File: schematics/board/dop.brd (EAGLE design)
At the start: 65.8 x 65.8 mm, 75 parts, among them X1 53047-02

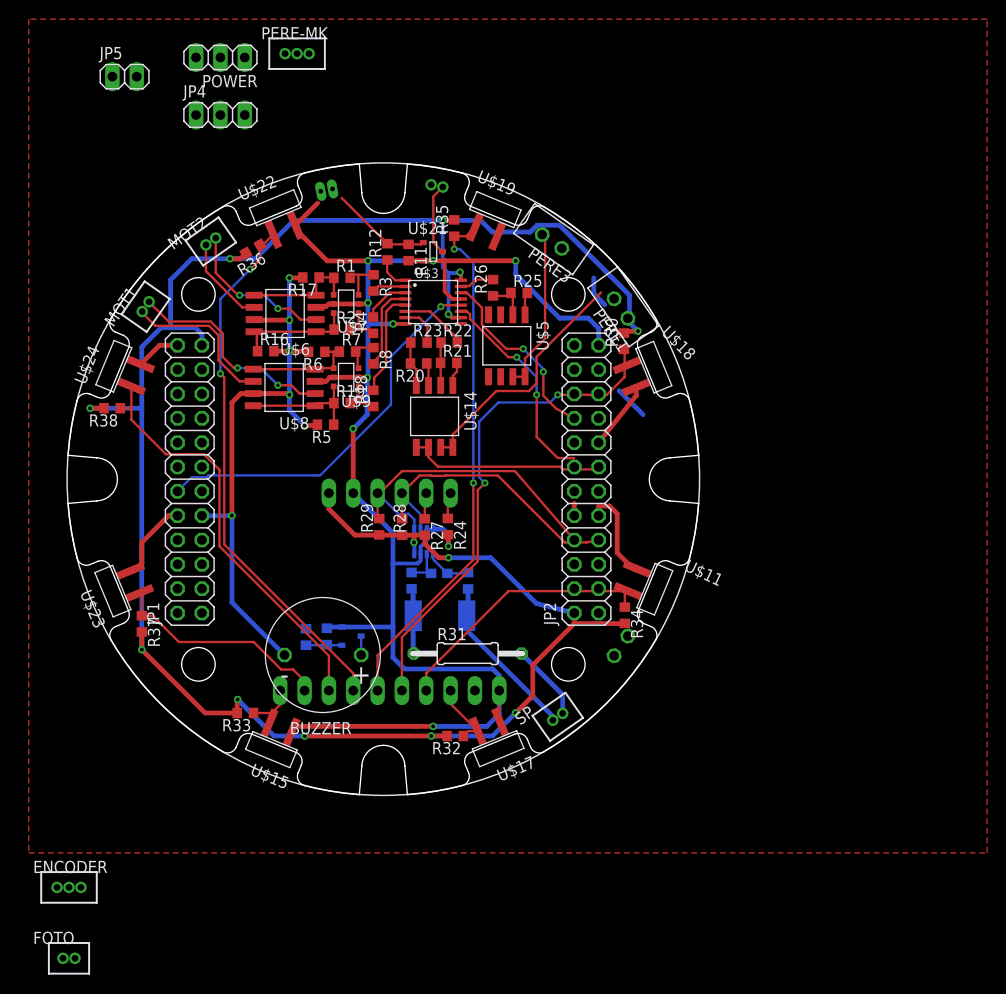
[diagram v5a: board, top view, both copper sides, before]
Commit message: Доделаны платы dop и mtr
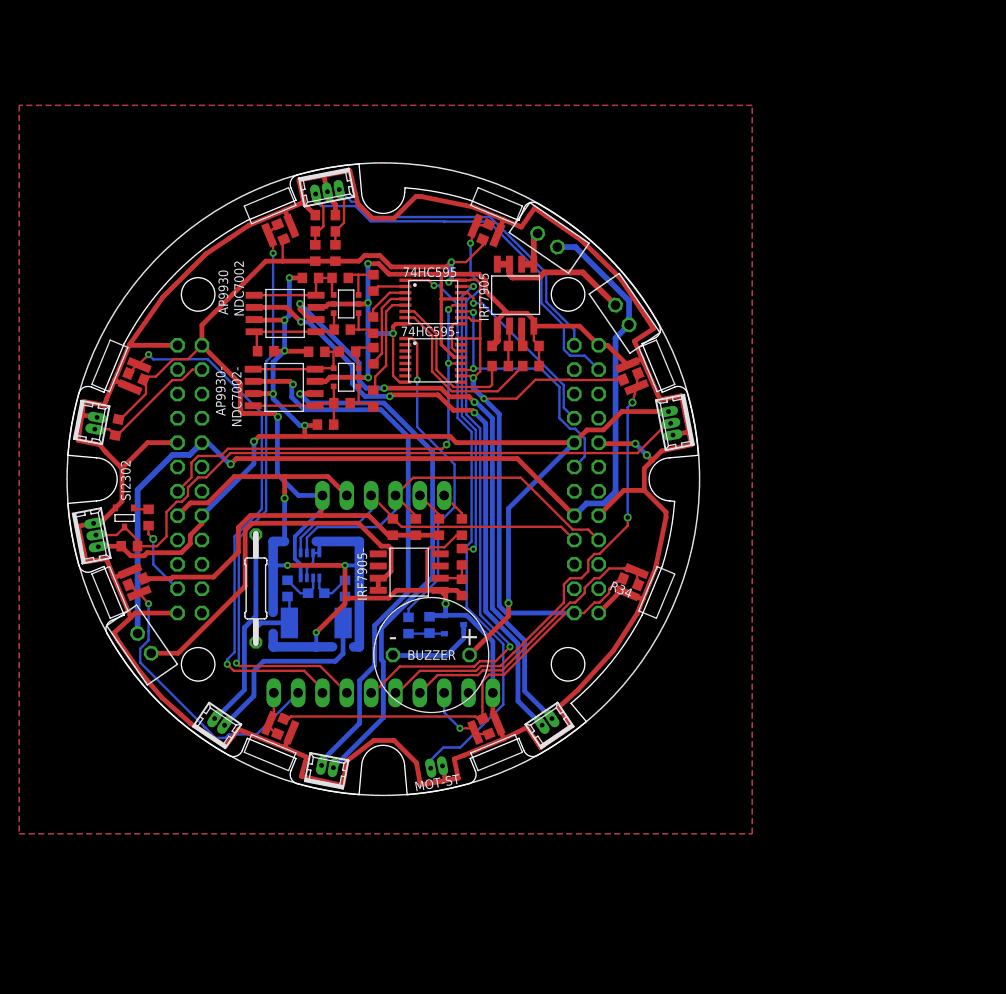
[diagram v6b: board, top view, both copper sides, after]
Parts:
- removed FOTO, MOT1, MOT2, MOT3: JST_2CON, CanCubeSat:JST_2CON_1.25
- removed JP4, POWER: (no value), pinhead:1X03
- removed JP5: (no value), pinhead:1X02
- removed PERE-MK: JST_3CON, CanCubeSat:JST_3CON_1.25
- removed PERE1, PERE2, PERE3: JST-2-2.5, CanCubeSat:JST-2-2.5
- removed U$14, U$5: IRF7905, CanCubeSat:SO8
- removed U$16: AD5593, CanCubeSat:AD5593
- removed U$2: INA219AID, CanCubeSat:INA219AID
- removed U$20, U$21: SI2302CDS, CanCubeSat:SI2302CDS
- removed U$3: 74HC595, CanCubeSat:74HC595
- removed X1: 53047-02, con-molex:53047-02
- added 74HC595, 74HC595-: 74HC595, CanCubeSat:TSSOP16
- added AD5593: AD5593, CanCubeSat:AD5593
- added C2, C3: 100nF, rcl:C0603
- added INA: INA219AID, CanCubeSat:SOT23-8
- added IRF7905, IRF7905-: IRF7905, CanCubeSat:SO8
- added LED, LED1: MOLEX-3-1.25, CanCubeSat:53047-03
- added MOT-H, MOT-ST, MOT-V, PHOTO: MOLEX-2-1.25, CanCubeSat:53047-02
- added PER-PAR, PER-SP, PER-ST: JST-2-2.5, CanCubeSat:JST-2-2.5
- added R39: 2k, rcl:R0603
- added R41: 100R, rcl:R0603
- added R42: 4k7, rcl:R0603
- added SI2302, SI2302-: SI2302CDS, CanCubeSat:SOT23-3
- ENCODER: value JST_3CON -> MOLEX-3-1.25; device CanCubeSat:JST_3CON_1.25 -> CanCubeSat:53047-03
- R11: value 10k -> 5k1
- R12: value 1k -> 5k1
- R16: value 10k -> 10k*3
- SP: value JST_2CON -> MOLEX-2-1.25; device CanCubeSat:JST_2CON_1.25 -> CanCubeSat:53047-02
- U$11, U$15, U$17, U$18, U$19, U$22, U$23, U$24: device CanCubeSat:VT93N1 -> KNPN-2023:VT93N1
- moved ENCODER 77.8 mm to (27.1, 63.4), turned to 191 degrees
- moved SP 35.5 mm to (15.7, 7.30), turned to 326 degrees
- moved R25 31.3 mm to (41.2, 21.7), turned to 270 degrees
- moved R26 28.3 mm to (41.2, 24.9)
- moved R31 23.1 mm to (19.7, 21.6), turned to 90 degrees
- moved C1 13.0 mm to (26.0, 21.1)
- moved R14 13.0 mm to (23.0, 21.6)
- moved R15 12.9 mm to (26.0, 18.0)
- moved R13 12.9 mm to (29.0, 21.6)
- moved R23 11.9 mm to (48.4, 44.8), turned to 180 degrees
- moved R20 11.9 mm to (48.4, 46.9), turned to 0 degrees
- moved BUZZER 11.3 mm to (38.0, 14.7), turned to 0 degrees
- moved R10 10.8 mm to (35.6, 17.7)
- moved R9 10.8 mm to (37.8, 17.8)
- moved R11 9.73 mm to (25.9, 56.6)
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- renumbered JP1 to A, JP2 to B, U$6 to AP9930, U$7 to NDC7002, U$8 to AP9930-, U$9 to NDC7002-
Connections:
- removed net ADC: JP5.2
- removed net CSK: JP4.2
- removed net ENCOD_C: ENCODER.1
- removed net FOTO_G: FOTO.3
- removed net FOTO_R: FOTO.2
- removed net I2C: JP5.1
- removed net MOTOR3-: MOT3.3, U$21.3
- removed net N$10: R21.2, U$14.1
- removed net N$11: R20.2, R23.1, U$14.4
- removed net N$19: R25.2, U$5.1
- removed net PA4: B.21
- removed net PA5: B.24
- removed net PA7: A.21
- removed net PA8: A.4
- new net FOTO9: A.22, PHOTO.1, R39.1
- new net LED: A.3, R41.1
- new net N$22: 74HC595-.14, 74HC595.9
- new net N$23: LED.2, LED1.2, R42.2, SI2302.3
- net 3V3: now also 74HC595-.10, 74HC595-.16, 74HC595.10, 74HC595.16, A.24, AD5593.16, B.1, INA.4, R11.2, R12.2, R39.2; no longer A.23, B.2, POWER.2, U$16.16, U$2.4, U$3.10, U$3.16
- net 5V: now also A.10, B.15, LED.1, LED1.1, R42.1; no longer A.9, B.16, POWER.1
- net BUZZER: now also 74HC595-.1
- net ENCOD_A: now also B.22, C3.2, ENCODER.1, R11.1; no longer ENCODER.2
- net ENCOD_B: now also B.23, C2.2, R12.1
- net FOTO1: now also AD5593.3; no longer U$16.3
- net FOTO2: now also AD5593.4, U$11.P$1; no longer U$11.P$2, U$16.4
- net FOTO3: now also AD5593.5, U$18.P$2; no longer U$16.5, U$18.P$1
- net FOTO4: now also AD5593.6; no longer U$16.6
- net FOTO5: now also AD5593.7; no longer U$16.7
- net FOTO6: now also AD5593.8, U$24.P$2; no longer U$16.8, U$24.P$1
- net FOTO7: now also AD5593.9; no longer U$16.9
- net FOTO8: now also AD5593.10; no longer U$16.10
- net GND: now also 74HC595-.13, 74HC595-.8, 74HC595.13, 74HC595.8, A.1, A.15, A.23, A.9, AD5593.1, AD5593.15, B.10, B.16, B.2, B.24, C2.1, C3.1, ENCODER.2, INA.3, INA.7, INA.8, IRF7905-.1, IRF7905.1, IRF7905.4, LED.3, LED1.3, MOT-ST.2, PHOTO.2, R20.2, R21.2, R23.1, R25.2, SI2302-.2, SI2302.2, U$11.P$2, U$18.P$1, U$24.P$1; no longer A.10, A.16, A.2, A.24, B.1, B.15, B.23, B.9, POWER.3, R11.2, U$11.P$1, U$16.1, U$16.15, U$18.P$2, U$2.3, U$2.7, U$2.8, U$20.2, U$21.2, U$24.P$2, U$3.13, U$3.8, X1.1
- net LATCH: now also 74HC595-.12, 74HC595.12, A.11; no longer A.12, JP4.3, U$3.12
- net MISO: now also B.18; no longer B.17
- net MK_MOTOR1+: now also 74HC595.4; no longer U$3.4
- net MK_MOTOR1-: now also 74HC595.5; no longer U$3.5
- net MK_MOTOR2+: now also 74HC595.2; no longer U$3.2
- net MK_MOTOR2-: now also 74HC595.3; no longer U$3.3
- net MOSI: now also 74HC595.14, B.17; no longer B.18, JP4.1, U$3.14
- net MOTOR1+: now also MOT-H.2; no longer MOT1.2
- net MOTOR1-: now also MOT-H.1; no longer MOT1.3
- net MOTOR2+: now also MOT-V.2; no longer MOT2.2
- net MOTOR2-: now also MOT-V.1; no longer MOT2.3
- net N$12: now also IRF7905.2; no longer U$14.2
- net N$13: now also SI2302-.3; no longer U$20.3
- net N$14: now also SI2302-.1; no longer U$20.1
- net N$15: now also INA.1; no longer U$2.1
- net N$16: now also INA.2; no longer U$2.2
- net N$17: now also R41.2, SI2302.1; no longer R11.1, R12.2, U$21.1, X1.2
- net N$18: now also AD5593.12; no longer U$16.12
- net N$20: now also AD5593.11; no longer U$16.11
- net N$21: now also IRF7905-.2; no longer U$5.2
- net N$9: now also IRF7905.3; no longer U$14.3
- net PA6: now also A.21; no longer A.22
- net PC5: now also A.20; no longer A.19
- net PERE1: now also 74HC595.6; no longer PERE-MK.2, U$3.6
- net PERE1_G: now also IRF7905.7, IRF7905.8, PER-PAR.1; no longer PERE1.1, U$14.7, U$14.8
- net PERE2: now also 74HC595.7; no longer PERE-MK.3, U$3.7
- net PERE2_G: now also IRF7905.5, IRF7905.6, PER-ST.1; no longer PERE2.2, U$14.5, U$14.6
- net PERE3: now also 74HC595.15; no longer PERE-MK.1, U$3.15
- net PERE3_G: now also IRF7905-.7, IRF7905-.8, PER-SP.1; no longer PERE3.1, U$5.7, U$5.8
- net SCK: now also 74HC595-.11, 74HC595.11, B.13; no longer B.14, U$3.11
- net SCL: now also AD5593.14, B.7, INA.5; no longer B.8, U$16.14, U$2.5
- net SDA: now also AD5593.13, B.8, INA.6; no longer B.7, U$16.13, U$2.6
- net SP+: now also SP.1; no longer SP.2
- net SP-: now also SP.2; no longer SP.3
- net TRUBKI: now also 74HC595.1, MOT-ST.1; no longer R12.1, U$3.1
- net VAB: now also A.16, B.9, PER-PAR.2, PER-SP.2, PER-ST.2; no longer A.15, B.10, PERE1.2, PERE2.1, PERE3.2
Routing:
- net GND: track 201.7 -> 508.7 mm, vias 9 -> 11
- net VAB: track 8.12 -> 101.9 mm, vias 0 -> 1
- net N$23: track 0.00 -> 68.8 mm
- net 5V: track 65.6 -> 126.4 mm, vias 6 -> 7
- net TRUBKI: track 3.53 -> 61.5 mm, vias 0 -> 1
- net MOTOR2+: track 9.33 -> 64.3 mm, vias 0 -> 3
- net ENCOD_A: track 0.00 -> 46.9 mm
- net MOTOR2-: track 16.1 -> 62.7 mm, vias 2 -> 3
- net MOTOR1+: track 16.2 -> 57.6 mm, vias 0 -> 1
- net ENCOD_B: track 0.00 -> 40.3 mm
- net BUZZER: track 0.00 -> 33.6 mm, vias 0 -> 1
- net MOTOR1-: track 22.7 -> 55.4 mm, vias 2 -> 1
- net PERE3: track 3.65 -> 31.2 mm, vias 0 -> 2
- net PERE3_G: track 16.4 -> 40.4 mm
- net PERE2_G: track 20.0 -> 4.64 mm
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- added copper zone on layer 16, net GND
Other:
- outline, holes or cut-outs redrawn
- board text added: "ENCODER"
- board text added: "LED1"
- board text added: "PER-PAR"
- board text added: "PER-ST"
- board text added: "PHOTO"

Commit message: Подготовлена плата dop
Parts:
- added R40: 10k, rcl:R0603
- moved PHOTO 43.8 mm to (38.9, 63.4), turned to 169 degrees
- moved R39 40.0 mm to (38.4, 60.8), turned to 349 degrees
- moved R41 1.00 mm to (8.50, 30.0)
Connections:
- removed net PA6: A.21
- removed net PC5: A.20
- new net SWITCH: B.22, R40.1
- net 3V3: now also R40.2
- net ENCOD_A: now also A.21; no longer B.22
- net ENCOD_B: now also A.22; no longer B.23
- net FOTO9: now also B.23; no longer A.22
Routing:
- net ENCOD_A: track 46.9 -> 30.6 mm
- net FOTO9: track 14.3 -> 25.5 mm
- net SWITCH: track 0.00 -> 8.66 mm, vias 0 -> 1
- net ENCOD_B: track 40.3 -> 32.8 mm
- net N$23: track 68.8 -> 71.3 mm
- net 3V3: track 238.6 -> 240.7 mm
- net FOTO2: track 29.9 -> 31.2 mm
- net LED: track 7.84 -> 9.13 mm
- net FOTO3: track 49.4 -> 50.7 mm
- net 5V: track 126.4 -> 125.4 mm
- net FOTO6: track 56.5 -> 57.1 mm
- net SCK: track 28.6 -> 29.1 mm
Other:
- outline, holes or cut-outs redrawn
